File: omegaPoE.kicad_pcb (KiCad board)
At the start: 4 copper layers, 32.5 x 48 mm, 84 parts, among them J1 RJ45-TRANS_POE, J2 CONN_EXPANSION, J3 Conn_02x01, J4 Conn_02x01, Q1 FDM3622, Q2 Q_NMOS_GSD, SW1 SW_Push, T1 PA1276, U1 LM5070, U2 PS2501-1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

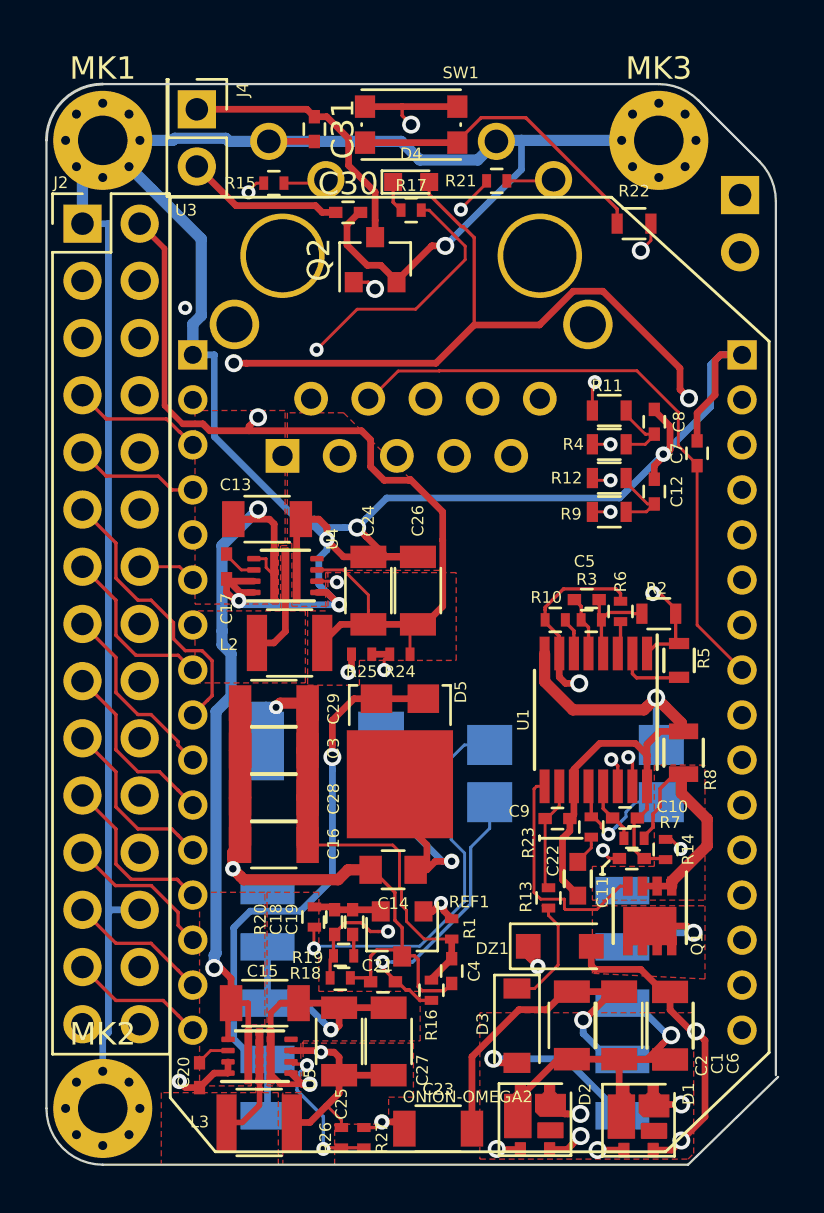
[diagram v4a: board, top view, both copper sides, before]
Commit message: Added silkscreen
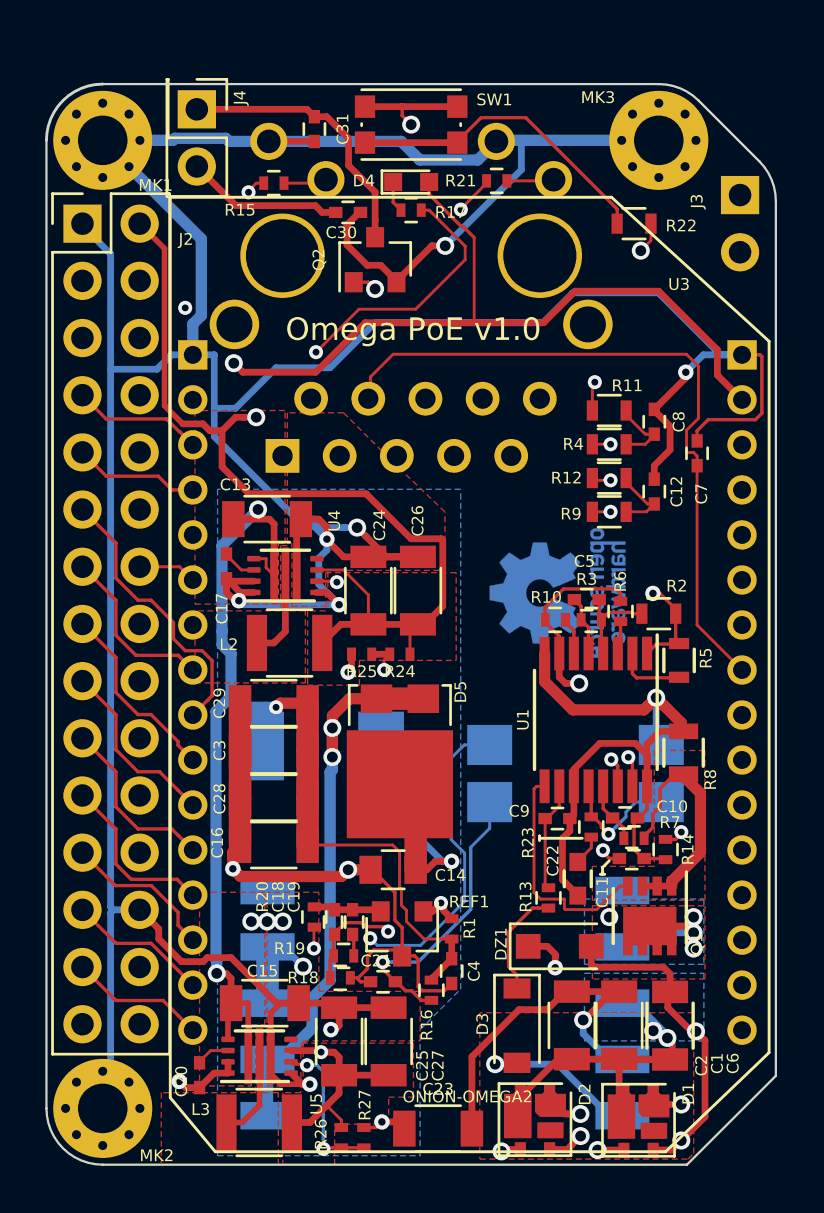
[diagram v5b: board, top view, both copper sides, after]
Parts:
- added REF**: KiCAD Logo, Symbols:Symbol_KiCAD-Logo_CopperAndSilkScreenTop, B.Cu at (112.2, 70.9)
- added REF***: OSHW-Logo_5.7x6mm_Copper, Symbols:OSHW-Logo_5.7x6mm_Copper, B.Cu at (107.2, 74.1)
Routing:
- net GND: track 261.3 -> 285.1 mm, vias 12 -> 17
- net /Input-48V: track 56.1 -> 51.8 mm
- net /NET_POW: track 27.6 -> 31.1 mm
- net GNDA: track 85.5 -> 83.4 mm, vias 2 -> 3
- net /IO19: track 31.8 -> 33.4 mm
- net Net-(D5-Pad1): track 26.1 -> 25.0 mm, vias 1 -> 2
- net /IO18: track 75.9 -> 76.9 mm
- net /Input_GND: track 72.7 -> 73.5 mm, vias 3 -> 4
- net /ETH_TD+: track 37.5 -> 36.7 mm
- net /freq_set: track 9.13 -> 8.41 mm
- net /ETH_TD-: track 33.6 -> 33.0 mm
- net /ETH_RD-: track 28.7 -> 29.3 mm
- net /Bridge1_2: track 37.9 -> 37.3 mm
- net Net-(R20-Pad2): track 16.9 -> 17.3 mm, vias 1 -> 2
- net +3V3: track 92.9 -> 93.2 mm, vias 3 -> 2
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- added copper zone on B.Cu, net /Input_GND
- added copper zone on B.Cu, net /coil_to_fet
- added copper zone on B.Cu, net GND
- added copper zone on In2.Cu, net GND
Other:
- board size 32.5 x 48 mm -> 32.4 x 48 mm
- board text added: "-48V"
- board text added: "0"
- board text added: "1"
- board text added: "12"
- board text added: "12V"
- board text added: "12V@1A 5V@2A 3.3V@2A"
- board text added: "13"
- board text added: "16"
- board text added: "17"
- board text added: "18"
- board text added: "19"
- board text added: "2"
- board text added: "2.5V"
- board text added: "3"
- board text added: "3.3V"
- board text added: "5V"
- board text added: "7"
- board text added: "8"
- board text added: "9"
- board text added: "G"
- board text added: "GND"
- board text added: "Non-isolated! PoE power!"
- board text added: "Omega PoE v1.0"
- board text added: "RB"
- board text added: "RX1"
- board text added: "S"
- board text added: "SCL"
- board text added: "SDA"
- board text added: "SwGND"
- board text added: "TX1"
- board text added: "U+"
- board text added: "U-"

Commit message: More cleanup. Fixing silkscreen on footprints, cleaing up MPN's.
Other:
- board text added: "http://github.com/zeroping/OmegaPoE"

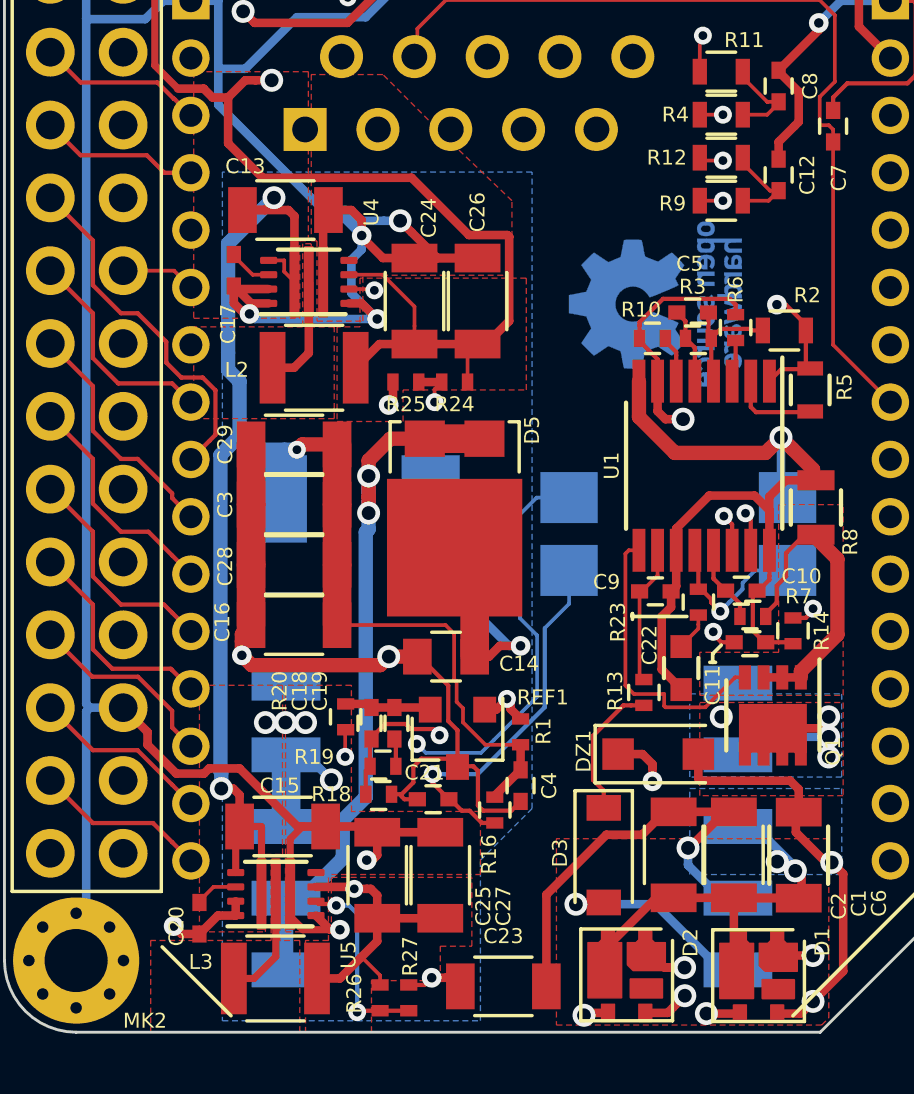
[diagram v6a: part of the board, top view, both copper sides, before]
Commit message: Moved flyback output components to minimize EMI. Lots of power flood work.
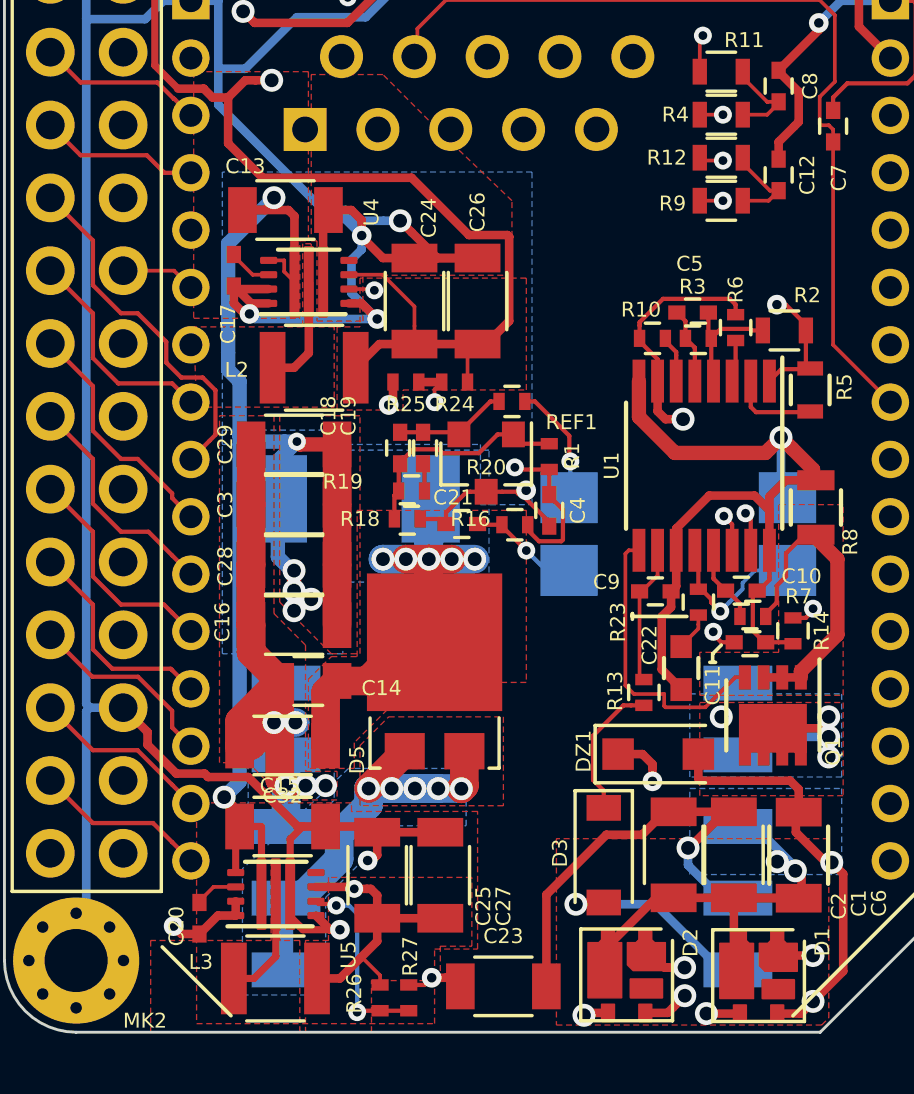
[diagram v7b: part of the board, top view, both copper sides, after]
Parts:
- removed REF**: KiCAD Logo, Symbols:Symbol_KiCAD-Logo_CopperAndSilkScreenTop
- removed REF***: OSHW-Logo_5.7x6mm_Copper, Symbols:OSHW-Logo_5.7x6mm_Copper
- added C32: DNP, Capacitors_SMD:C_1206, F.Cu at (94.2, 89.5)
- moved R20 12.4 mm to (102.2, 77.5), turned to 0 degrees
- moved R16 9.97 mm to (102.3, 81.8), turned to 180 degrees
- moved C4 9.65 mm to (103.5, 81.3)
- moved R1 9.65 mm to (103.5, 79.4)
- moved R18 9.65 mm to (98.5, 81.6)
- moved C18 9.65 mm to (98.3, 79.1)
- moved C19 9.65 mm to (99.1, 79.1)
- moved C21 9.65 mm to (100.5, 81.8)
- moved R19 9.65 mm to (98.7, 80.6)
- moved REF1 9.65 mm to (101.3, 79.7)
- moved D5 7.13 mm to (99.5, 87.8), turned to 180 degrees
- moved C14 4.87 mm to (95.1, 87.2)
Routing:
- net Net-(R20-Pad2): track 17.3 -> 4.24 mm, vias 2 -> 1
- net Net-(C21-Pad1): track 13.3 -> 3.89 mm
- net +12V: track 83.3 -> 92.2 mm, vias 3 -> 8
- net Net-(D5-Pad1): track 25.0 -> 16.7 mm, vias 2 -> 5
- net GND: track 285.1 -> 281.3 mm
- net /output_pre_choke: track 12.5 -> 15.9 mm, vias 1 -> 5
- net Net-(C18-Pad1): track 9.28 -> 7.91 mm, vias 2 -> 0
- net Net-(C18-Pad2): track 3.03 -> 3.99 mm
- net /IO4: track 31.3 -> 31.9 mm
- net /IO19: track 33.4 -> 32.8 mm
- added copper zone on B.Cu, net +12V
- added copper zone on B.Cu, net /output_pre_choke
- added copper zone on F.Cu, net /output_pre_choke
- added copper zone on B.Cu, net Net-(D5-Pad1)
- added copper zone on F.Cu, net Net-(D5-Pad1)

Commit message: Not sure what changed - more zone cleanup, I think?
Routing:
- net GNDA: track 83.4 -> 87.2 mm
- added copper zone on F.Cu, net GNDA
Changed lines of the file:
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@@
     (thickness 1.6)
     (drawings 62)
-    (tracks 1230)
+    (tracks 1234)
     (zones 0)
     (modules 85)
@@
   (page A3)
   (layers
-    (0 F.Cu signal)
-    (1 In1.Cu power)
-    (2 In2.Cu signal hide)
-    (31 B.Cu signal hide)
+    (0 F.Cu signal hide)
+    (1 In1.Cu power hide)
+    (2 In2.Cu signal)
+    (31 B.Cu signal)
     (32 B.Adhes user hide)
     (33 F.Adhes user hide)
@@
   )
   (setup
-    (last_trace_width 0.5)
+    (last_trace_width 0.3)
     (user_trace_width 0.15)
     (user_trace_width 0.25)
@@
   (segment (start 109.950789 94.825) (end 109.938603 94.812814) (width 0.3) (layer F.Cu) (net 2) (status 30))
   (segment (start 110.08 92.325) (end 109.49 92.325) (width 0.4) (layer B.Cu) (net 2) (status 30))
+  (segment (start 111.1781 80.8219) (end 111.1781 80.7219) (width 0.5) (layer F.Cu) (net 3))
+  (segment (start 111.1781 80.7219) (end 111.65 80.25) (width 0.5) (layer F.Cu) (net 3))
+  (segment (start 111.65 80.25) (end 112.8 80.25) (width 0.5) (layer F.Cu) (net 3))
+  (segment (start 111.1781 82.692351) (end 111.1781 80.8219) (width 0.5) (layer F.Cu) (net 3))
   (segment (start 111.5 71.9) (end 111.5 63.5) (width 0.3) (layer In1.Cu) (net 3))
   (segment (start 112.090944 72.490944) (end 111.5 71.9) (width 0.3) (layer In1.Cu) (net 3))
@@
     (polygon
       (pts
-        (xy 84.8 99.2) (xy 101 99.2) (xy 101 93.5) (xy 103 91.5) (xy 103 70.9)
+        (xy 84.8 99.2) (xy 101 99.2) (xy 101 91.5) (xy 103 89.5) (xy 103 70.9)
         (xy 101 68.9) (xy 101 67.2) (xy 102.3 65.9) (xy 102.3 64.7) (xy 103 64)
         (xy 107.5 64) (xy 110.1 61.4) (xy 110.1 51.8) (xy 84.8 51.8)
@@
     )
   )
-  (zone (net 1) (net_name GND) (layer B.Cu) (hatch edge 0.508)
-    (priority 4)
-    (connect_pads yes (clearance 0.15))
-    (min_thickness 0.15)
-    (fill yes (arc_segments 16) (thermal_gap 0.508) (thermal_bridge_width 0.508))
-    (polygon
-      (pts
-        (xy 101.1 79) (xy 101.1 81.1) (xy 102.9 81.1) (xy 102.9 69.5) (xy 92.1 69.5)
-        (xy 92.1 79)
-      )
-    )
-  )
   (zone (net 1) (net_name GND) (layer In2.Cu) (hatch edge 0.508)
     (priority 4)
@@
       )
     )
+  )
+  (zone (net 1) (net_name GND) (layer B.Cu) (hatch edge 0.508)
+    (connect_pads thru_hole_only (clearance 0.15))
+    (min_thickness 0.15)
+    (fill yes (arc_segments 16) (thermal_gap 0.508) (thermal_bridge_width 0.508))
+    (polygon
+      (pts
+        (xy 84.8 99.2) (xy 101 99.2) (xy 101 91.5) (xy 103 89.5) (xy 103 70.9)
+        (xy 100.8 68.7) (xy 100.8 67) (xy 102.1 65.7) (xy 102.1 64.9) (xy 103 64)
+        (xy 107.5 64) (xy 110.1 61.4) (xy 110.1 51.8) (xy 84.8 51.8)
+      )
+    )
+  )
+  (zone (net 3) (net_name GNDA) (layer F.Cu) (hatch edge 0.508)
+    (priority 14)
+    (connect_pads yes (clearance 0.15))
+    (min_thickness 0.254)
+    (fill yes (arc_segments 16) (thermal_gap 0.508) (thermal_bridge_width 0.508))
+    (polygon
+      (pts
+        (xy 106 75.8) (xy 107 75.8) (xy 107 77.7) (xy 113.7 77.7) (xy 113.7 80.9)
+        (xy 111.4 80.9) (xy 110.7 80.2) (xy 106 80.2)
+      )
+    )
